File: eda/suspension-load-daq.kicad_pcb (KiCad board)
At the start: 4 copper layers, 252 parts, among them IC1 ICM-42688-P, J1 B3B-PH-K-S, J10 B6B-PH-K-S, J11 B6B-PH-K-S, J12 B6B-PH-K-S, J13 2.54mm 5 x 2 THT Vertical Male, J14 TC2030-NL_CTX, J15 USB4105, J16 B4B-PH-K-S, J17 DM3D-SF, J2 B3B-PH-K-S, J3 B3B-PH-K-S, J4 B3B-PH-K-S, J5 B6B-PH-K-S, J6 B6B-PH-K-S, J7 B6B-PH-K-S, J8 B6B-PH-K-S, J9 B6B-PH-K-S, Q1 PJE138K_R1_00001, Q2 PJE138K_R1_00001, Q3 PJE138K_R1_00001, Q4 PJE138K_R1_00001, Q5 PJE138K_R1_00001, Q6 PJE138K_R1_00001, Q7 PJE138K_R1_00001, Q8 PJE138K_R1_00001, SW1 KMR211NGLFS, U1 TCAN1462VDRBRQ1, U2 LT3042xMSE, U3 STM32F412CEU6, U4 TPSM33610S5QRDNRQ1, U5 TPS74501PDRVR, U6 LP5907MFX-3.3, U7 ADS131M08xPBS, Y1 8MHz 10pF

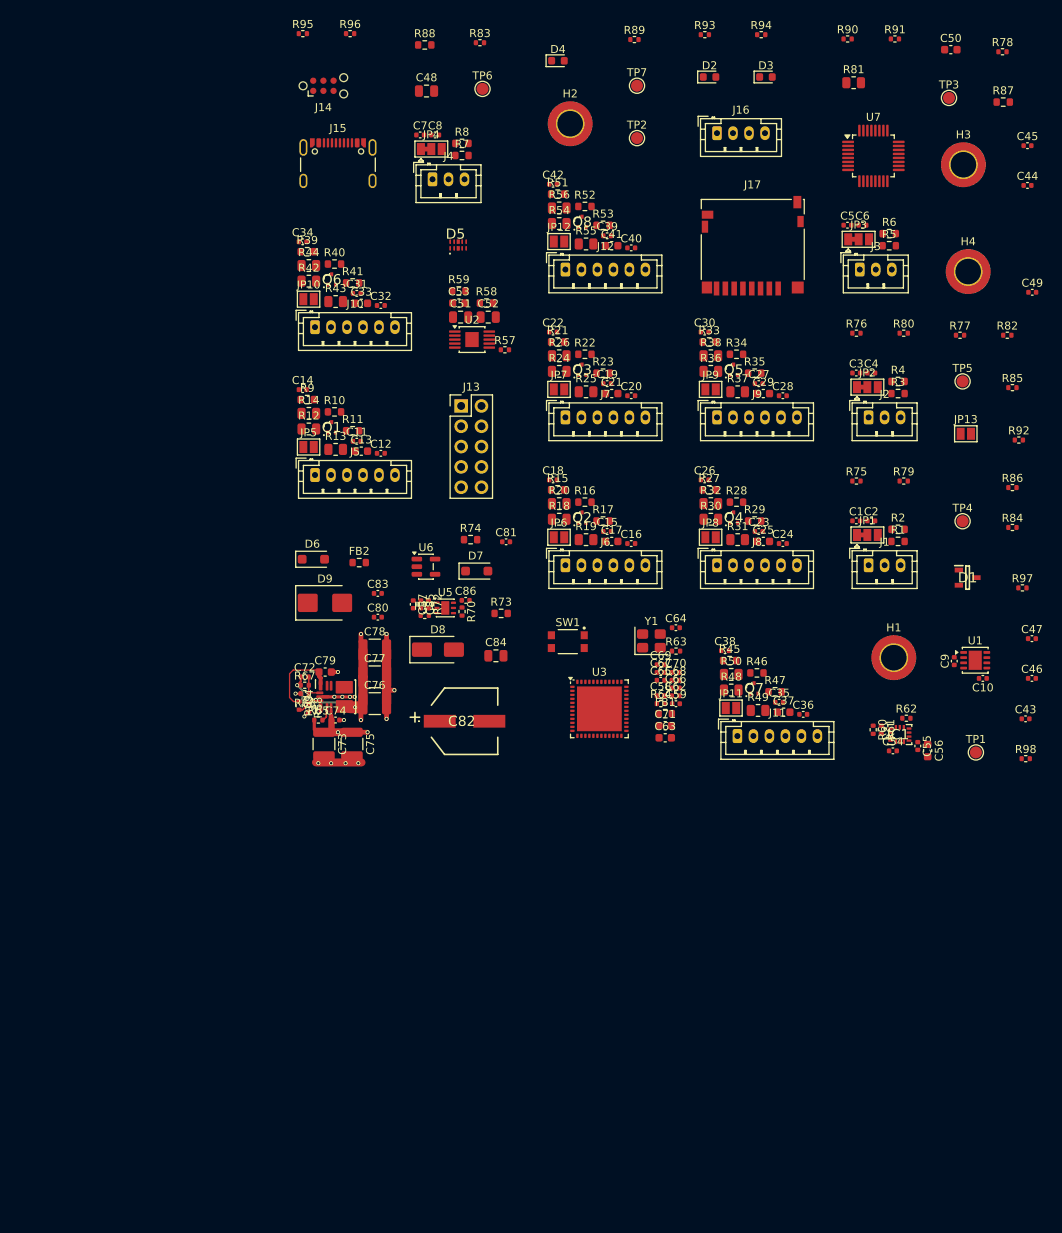
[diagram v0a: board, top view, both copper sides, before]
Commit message: Add Rev B: routed layout and fab package (Diode 99bcdad)
Imports the completed Rev B board from code.diode.computer/lena/b/string-gauge-daq
at commit 99bcdad.

- Design source: placed, routed and poured 99 x 76 mm 4-layer layout
  (DRC 0 errors / 0 unconnected), AUX fault clamps D10-D13, D6/D7 changed to
  RB168MM-40 (1A_40V_LowIR replaces 1A_20V), ICM-42688-P symbol update.
  pcb build: 256 components.
- fab/rev-b/: JLCPCB Gerber zip, Gerbers/drills, BOM/CPL, schematic/assembly
  PDFs, DRC/ERC reports, STEP, IPC-2581, renders. MANIFEST.txt holds SHA-256
  sums (verified on import).
- spec.md/README.md: Rev B layout and status merged with this repo's own
  edits (test-plan and board-spec references, aux sensor options, run
  metadata).
- .gitignore: anchor docs/ to the repo root so fab/rev-b/docs/ is tracked;
  .gitattributes: store fab/ byte-for-byte.

Not imported: Diode-only import/validation JSONs, the Rev-A KiCad archive zip,
.lfsconfig, and the unused STM32F446RETx symbol.

Co-Authored-By: Claude Opus 5.5 <noreply@anthropic.com>
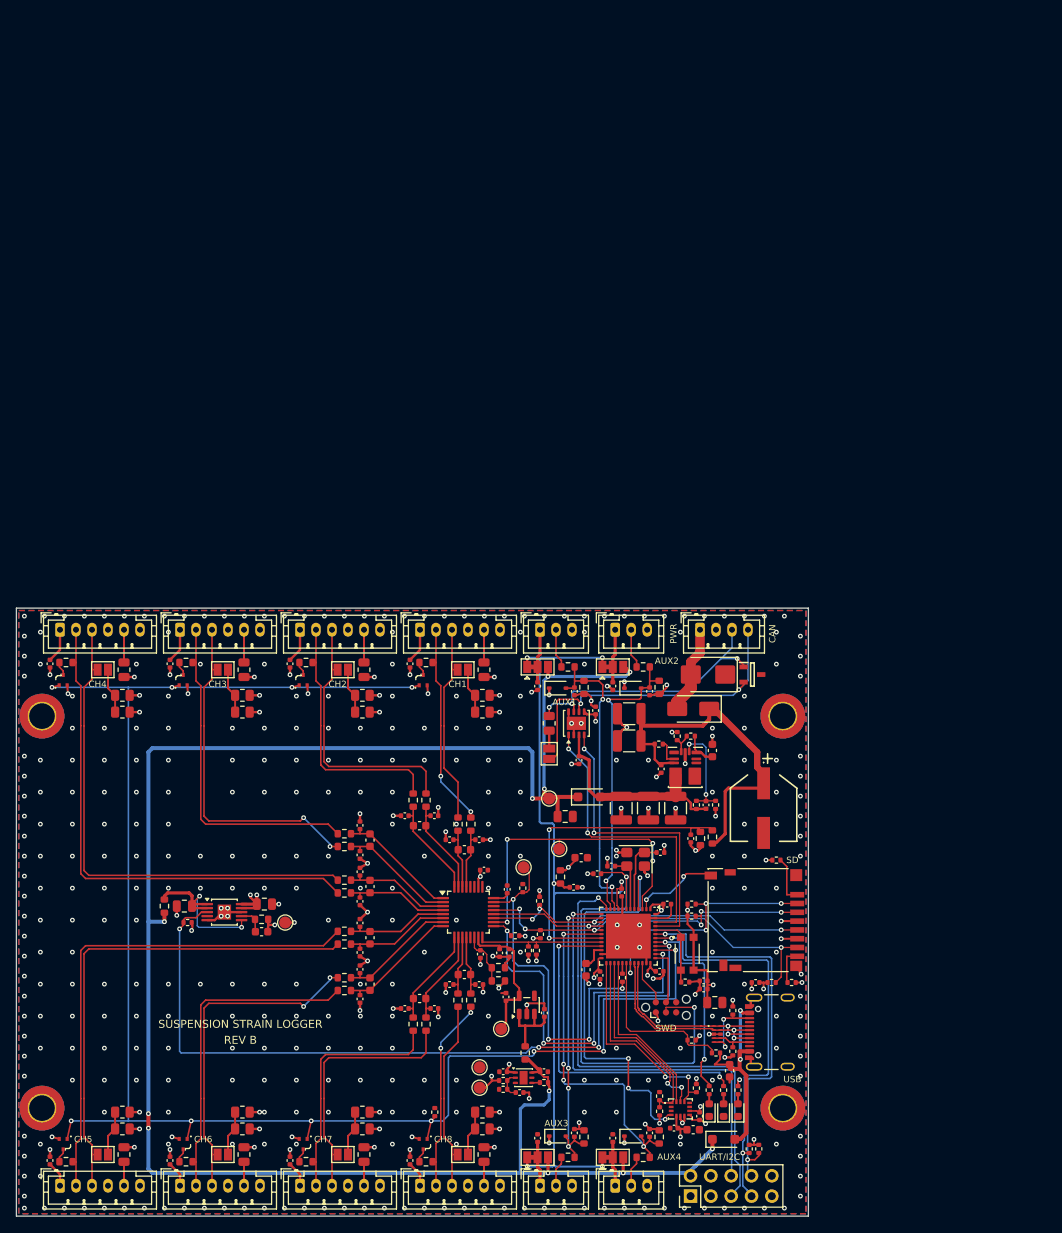
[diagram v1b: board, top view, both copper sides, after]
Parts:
- added D10: 200mA 30V Schottky Rectifier, stdlib_kicad-footprints_Diode_SMD:D_SOD-323, F.Cu at (167.7, 110.0)
- added D11: 200mA 30V Schottky Rectifier, stdlib_kicad-footprints_Diode_SMD:D_SOD-323, F.Cu at (177.1, 110.0)
- added D12: 200mA 30V Schottky Rectifier, stdlib_kicad-footprints_Diode_SMD:D_SOD-323, F.Cu at (167.7, 166.0)
- added D13: 200mA 30V Schottky Rectifier, stdlib_kicad-footprints_Diode_SMD:D_SOD-323, F.Cu at (177.1, 166.0)
- D6, D7: value 1A 20V Schottky Rectifier -> 1A 40V Low-IR Schottky; footprint lena_b_string-gauge-daq_components_1A_20V_Schottky_Rectifier:D_SOD-123F -> lena_b_string-gauge-daq_components_1A_40V_LowIR_Schottky_Rectifier:D_SOD-123F
- moved H3 164.8 mm to (103.2, 162.5)
- moved R89 139.4 mm to (191.6, 167.6), turned to 90 degrees
- moved R90 139.2 mm to (192.8, 167.6), turned to 90 degrees
- moved R96 135.2 mm to (152.3, 163.0), turned to 90 degrees
- moved D4 133.1 mm to (190.2, 162.7), turned to 90 degrees
- moved TP3 132.3 mm to (133.6, 139.3)
- moved C30 132.0 mm to (104.2, 169.1), turned to 90 degrees
- moved C50 130.6 mm to (189.2, 157.8), turned to -90 degrees
- moved R33 130.3 mm to (106.2, 169.2), turned to 180 degrees
- moved D3 129.2 mm to (188.4, 162.7), turned to 90 degrees
- moved D2 129.1 mm to (186.6, 162.7), turned to 90 degrees
- moved R8 128.7 mm to (178.3, 168.7)
- moved JP4 128.1 mm to (174.6, 168.7)
- moved Q5 128.0 mm to (105.8, 167.0), turned to 180 degrees
- moved C7 128.0 mm to (179.2, 165.6), turned to 90 degrees
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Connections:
- H1 pad 1: B9855FCC_4E57_56EE_A9F9_C8367AF65EAF./H1_P1 -> GND
- H2 pad 1: SHEET_559955D8_FA6E_5336_B163_4DA49DAC212C./H2_P1 -> GND
- H3 pad 1: CC7E77AF_AAD5_5431_9019_5B31A35F631D./H3_P1 -> GND
- H4 pad 1: SHEET_2F326288_1754_5D21_977F_834F10F62F25./H4_P1 -> GND
- IC1 pad 9: SHEET_8522DDAD_AE9A_56B5_B069_4220863B1849.IC1.NC_ICM-42688-P_INT2_/_FSYNC_/_CLKIN -> GND
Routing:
- net V5: track 0.00 -> 243.3 mm, vias 0 -> 11
- net /SHUNT_CAL: track 0.00 -> 211.4 mm, vias 0 -> 11
- net GND: track 21.7 -> 131.1 mm, vias 15 -> 426
- net VDDA: track 0.00 -> 104.3 mm, vias 0 -> 6
- net /EXC_EN: track 0.00 -> 95.7 mm, vias 0 -> 4
- net /CH3_IN_P: track 0.00 -> 64.3 mm
- net /CH3_IN_N: track 0.00 -> 63.4 mm
- net /CH4_IN_P: track 0.00 -> 63.2 mm
- net /CH4_IN_N: track 0.00 -> 62.3 mm
- net /UART_TX: track 0.00 -> 61.1 mm, vias 0 -> 1
- net /NRST: track 0.00 -> 61.1 mm, vias 0 -> 2
- net /UART_RX: track 0.00 -> 55.6 mm, vias 0 -> 1
- net V3V3: track 0.00 -> 54.8 mm, vias 0 -> 28
- net IMU_INT1: track 0.00 -> 51.0 mm, vias 0 -> 4
- net /I2C_SCL: track 0.00 -> 49.8 mm, vias 0 -> 2
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- added copper zone on In2.Cu, net EXC
- added copper zone on B.Cu, net GND
- added copper zone on F.Cu, net GND
- added copper zone on In1.Cu, net GND
- added copper zone on In2.Cu, net V3V3
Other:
- board outline added: 99 x 76 mm
- board text added: "AUX1"
- board text added: "AUX2"
- board text added: "AUX3"
- board text added: "AUX4"
- board text added: "CAN"
- board text added: "CH1"
- board text added: "CH2"
- board text added: "CH3"
- board text added: "CH4"
- board text added: "CH5"
- board text added: "CH6"
- board text added: "CH7"
- board text added: "CH8"
- board text added: "PWR"
- board text added: "REV B"
- board text added: "SD"
- board text added: "SUSPENSION STRAIN LOGGER"
- board text added: "SWD"
- board text added: "UART/I2C"
- board text added: "USB"
